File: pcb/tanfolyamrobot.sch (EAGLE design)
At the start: 80 parts, among them IC1 STM32F10XRXT6, IC2 7805, IC4 FT232RL, IC5 LD117AS33TR, M1 DRV8833, Q1 16MHz, Q2 BSS123, Q3 BSS123, Q4 BSS123, X2 PWR, X6 KUSBVX-BS1N

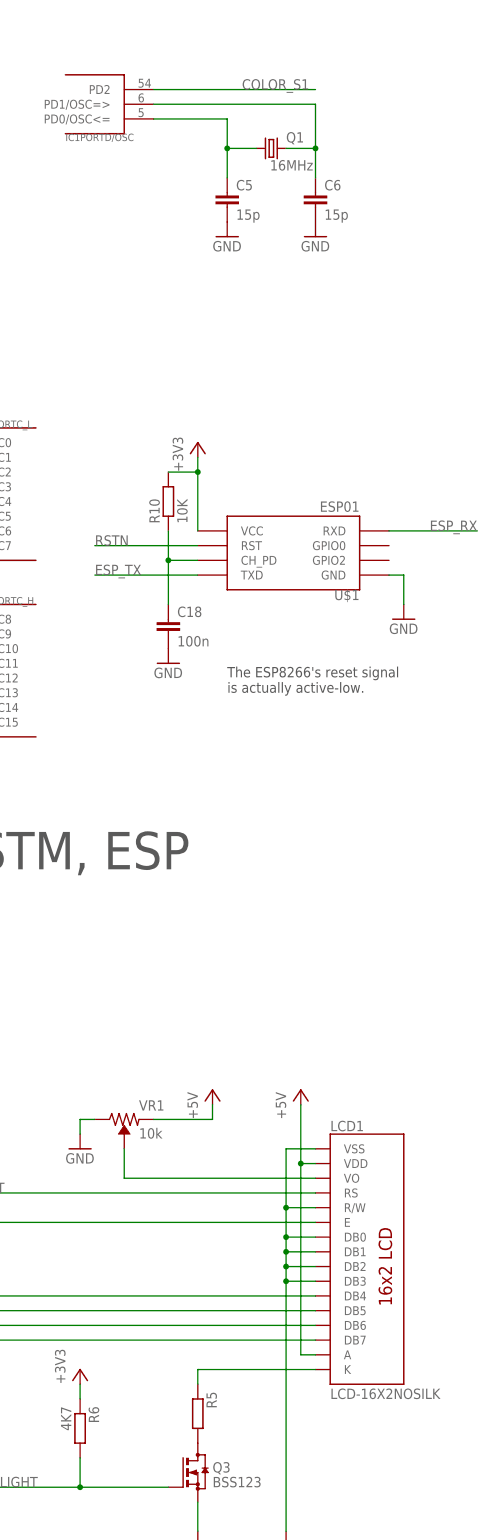
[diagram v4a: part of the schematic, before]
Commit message: changed xtal to smd resonator (#1)
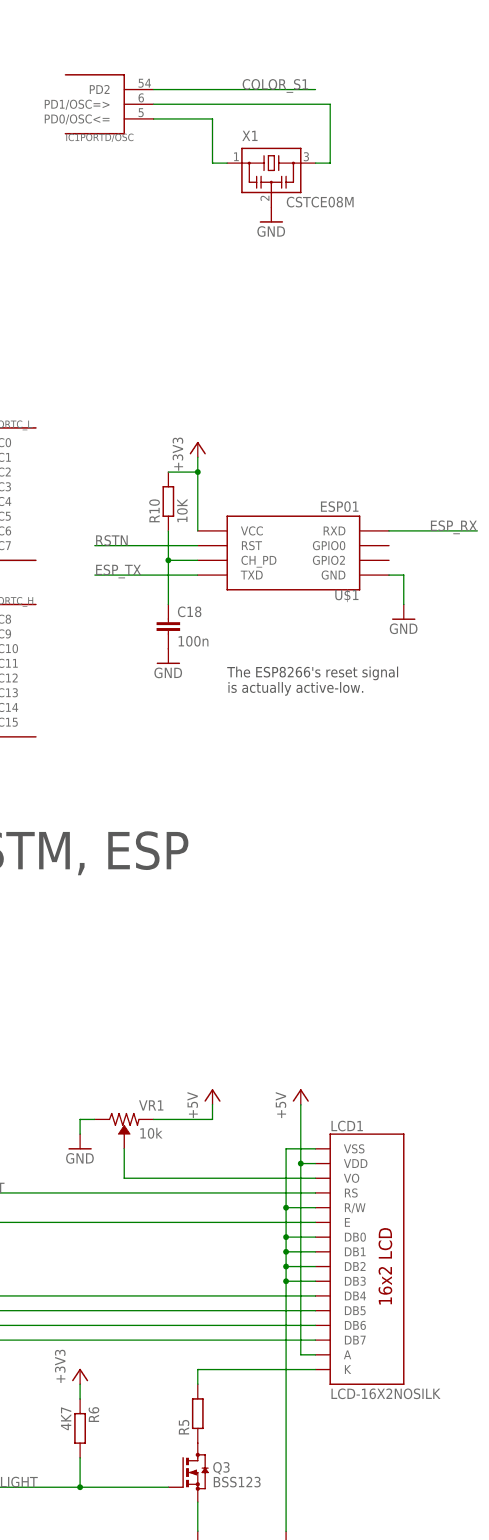
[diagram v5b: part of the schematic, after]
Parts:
- removed C5, C6: 15p, rcl:C-EUC0603
- removed Q1: 16MHz, crystal:CRYSTALHC49U-V
- added X1: CSTCE08M, resonator:MURATA_CSTCE
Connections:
- removed net LCD_K: LCD1.K, R5.1
- new net N$6: LCD1.K, R5.2
- net GND: now also X1.2; no longer C5.2, C6.2
- net N$1: now also R5.1; no longer R5.2
- net OSCIN: now also X1.1; no longer C5.1, Q1.1
- net OSCOUT: now also X1.3; no longer C6.1, Q1.2
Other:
- moved on the sheet: R5
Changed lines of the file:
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@@
 <part name="C3" library="rcl" library_urn="urn:adsk.eagle:library:334" deviceset="C-EU" device="C0603" package3d_urn="urn:adsk.eagle:package:23616/2" value="100n"/>
 <part name="C4" library="rcl" library_urn="urn:adsk.eagle:library:334" deviceset="C-EU" device="C0603" package3d_urn="urn:adsk.eagle:package:23616/2" value="100n"/>
-<part name="Q1" library="crystal" library_urn="urn:adsk.eagle:library:204" deviceset="CRYSTAL" device="HC49U-V" package3d_urn="urn:adsk.eagle:package:12075/1" value="16MHz"/>
-<part name="C5" library="rcl" library_urn="urn:adsk.eagle:library:334" deviceset="C-EU" device="C0603" package3d_urn="urn:adsk.eagle:package:23616/2" value="15p"/>
-<part name="C6" library="rcl" library_urn="urn:adsk.eagle:library:334" deviceset="C-EU" device="C0603" package3d_urn="urn:adsk.eagle:package:23616/2" value="15p"/>
-<part name="GND2" library="supply1" library_urn="urn:adsk.eagle:library:371" deviceset="GND" device=""/>
-<part name="GND3" library="supply1" library_urn="urn:adsk.eagle:library:371" deviceset="GND" device=""/>
 <part name="GND4" library="supply1" library_urn="urn:adsk.eagle:library:371" deviceset="GND" device=""/>
 <part name="+3V2" library="supply1" library_urn="urn:adsk.eagle:library:371" deviceset="+3V3" device=""/>
@@
 <part name="R27" library="rcl" library_urn="urn:adsk.eagle:library:334" deviceset="R-EU_" device="R0603" package3d_urn="urn:adsk.eagle:package:23555/3" value="0R"/>
 <part name="R28" library="rcl" library_urn="urn:adsk.eagle:library:334" deviceset="R-EU_" device="R0603" package3d_urn="urn:adsk.eagle:package:23555/3" value="0R"/>
+<part name="X1" library="resonator" deviceset="MURATA_CSTCE" device="" value="CSTCE08M"/>
+<part name="GND2" library="supply1" library_urn="urn:adsk.eagle:library:371" deviceset="GND" device=""/>
 </parts>
 <sheets>
@@
 <attribute name="VALUE" x="329.184" y="317.881" size="1.778" layer="96"/>
 </instance>
-<instance part="Q1" gate="G$1" x="487.68" y="322.58" smashed="yes">
-<attribute name="NAME" x="490.22" y="323.596" size="1.778" layer="95"/>
-<attribute name="VALUE" x="487.426" y="318.77" size="1.778" layer="96"/>
-</instance>
-<instance part="C5" gate="G$1" x="480.06" y="314.96" smashed="yes">
-<attribute name="NAME" x="481.584" y="315.341" size="1.778" layer="95"/>
-<attribute name="VALUE" x="481.584" y="310.261" size="1.778" layer="96"/>
-</instance>
-<instance part="C6" gate="G$1" x="495.3" y="314.96" smashed="yes">
-<attribute name="NAME" x="496.824" y="315.341" size="1.778" layer="95"/>
-<attribute name="VALUE" x="496.824" y="310.261" size="1.778" layer="96"/>
-</instance>
-<instance part="GND2" gate="1" x="480.06" y="307.34" smashed="yes">
-<attribute name="VALUE" x="477.52" y="304.8" size="1.778" layer="96"/>
-</instance>
-<instance part="GND3" gate="1" x="495.3" y="307.34" smashed="yes">
-<attribute name="VALUE" x="492.76" y="304.8" size="1.778" layer="96"/>
-</instance>
 <instance part="GND4" gate="1" x="391.16" y="309.88" smashed="yes">
 <attribute name="VALUE" x="388.62" y="307.34" size="1.778" layer="96"/>
@@
 <attribute name="VALUE" x="487.68" y="78.74" size="1.778" layer="96"/>
 </instance>
-<instance part="R5" gate="G$1" x="474.98" y="104.14" smashed="yes" rot="R270">
-<attribute name="NAME" x="476.4786" y="107.95" size="1.778" layer="95" rot="R270"/>
-<attribute name="VALUE" x="471.678" y="107.95" size="1.778" layer="96" rot="R270"/>
+<instance part="R5" gate="G$1" x="474.98" y="104.14" smashed="yes" rot="R90">
+<attribute name="NAME" x="473.4814" y="100.33" size="1.778" layer="95" rot="R90"/>
+<attribute name="VALUE" x="478.282" y="100.33" size="1.778" layer="96" rot="R90"/>
 </instance>
 <instance part="R6" gate="G$1" x="454.66" y="101.6" smashed="yes" rot="R270">
@@
 <attribute name="NAME" x="138.43" y="280.8986" size="1.778" layer="95"/>
 <attribute name="VALUE" x="144.526" y="280.924" size="1.778" layer="96"/>
+</instance>
+<instance part="X1" gate="G$1" x="487.68" y="320.04" smashed="yes">
+<attribute name="NAME" x="482.6" y="323.85" size="1.778" layer="95"/>
+<attribute name="VALUE" x="490.22" y="312.42" size="1.778" layer="96"/>
+</instance>
+<instance part="GND2" gate="1" x="487.68" y="309.88" smashed="yes">
+<attribute name="VALUE" x="485.14" y="307.34" size="1.778" layer="96"/>
 </instance>
 </instances>
@@
 </segment>
 <segment>
-<pinref part="C5" gate="G$1" pin="2"/>
-<pinref part="GND2" gate="1" pin="GND"/>
-</segment>
-<segment>
-<pinref part="C6" gate="G$1" pin="2"/>
-<pinref part="GND3" gate="1" pin="GND"/>
-</segment>
-<segment>
 <pinref part="C7" gate="G$1" pin="2"/>
 <wire x1="391.16" y1="314.96" x2="391.16" y2="317.5" width="0.1524" layer="91"/>
@@
 <pinref part="R9" gate="G$1" pin="2"/>
 <pinref part="GND35" gate="1" pin="GND"/>
+</segment>
+<segment>
+<pinref part="X1" gate="G$1" pin="2"/>
+<pinref part="GND2" gate="1" pin="GND"/>
 </segment>
 </net>
@@
 </segment>
 </net>
-<net name="OSCOUT" class="0">
-<segment>
-<wire x1="495.3" y1="330.2" x2="495.3" y2="322.58" width="0.1524" layer="91"/>
-<pinref part="Q1" gate="G$1" pin="2"/>
-<wire x1="490.22" y1="322.58" x2="495.3" y2="322.58" width="0.1524" layer="91"/>
-<wire x1="495.3" y1="322.58" x2="495.3" y2="317.5" width="0.1524" layer="91"/>
-<junction x="495.3" y="322.58"/>
-<pinref part="C6" gate="G$1" pin="1"/>
-<pinref part="IC1" gate="PORTD/OSC" pin="PD1/OSC=&gt;"/>
-<wire x1="467.36" y1="330.2" x2="495.3" y2="330.2" width="0.1524" layer="91"/>
-</segment>
-</net>
-<net name="OSCIN" class="0">
-<segment>
-<pinref part="Q1" gate="G$1" pin="1"/>
-<wire x1="485.14" y1="322.58" x2="480.06" y2="322.58" width="0.1524" layer="91"/>
-<wire x1="480.06" y1="322.58" x2="480.06" y2="317.5" width="0.1524" layer="91"/>
-<pinref part="C5" gate="G$1" pin="1"/>
-<wire x1="480.06" y1="327.66" x2="480.06" y2="322.58" width="0.1524" layer="91"/>
-<junction x="480.06" y="322.58"/>
-<pinref part="IC1" gate="PORTD/OSC" pin="PD0/OSC&lt;="/>
-<wire x1="467.36" y1="327.66" x2="480.06" y2="327.66" width="0.1524" layer="91"/>
-</segment>
-</net>
 <net name="SWD_SWO" class="0">
 <segment>
@@
 <wire x1="370.84" y1="238.76" x2="347.98" y2="238.76" width="0.1524" layer="91"/>
 <label x="347.98" y="238.76" size="1.778" layer="95"/>
-</segment>
-</net>
-<net name="LCD_K" class="0">
-<segment>
-<pinref part="R5" gate="G$1" pin="1"/>
-<wire x1="474.98" y1="109.22" x2="474.98" y2="111.76" width="0.1524" layer="91"/>
-<pinref part="LCD1" gate="G$1" pin="K"/>
-<wire x1="474.98" y1="111.76" x2="495.3" y2="111.76" width="0.1524" layer="91"/>
 </segment>
 </net>
@@
 </segment>
 </net>
-<net name="N$1" class="0">
-<segment>
-<pinref part="R5" gate="G$1" pin="2"/>
-<pinref part="Q3" gate="G$1" pin="D"/>
-</segment>
-</net>
 <net name="BOOT0" class="0">
 <segment>
@@
 </segment>
 </net>
+<net name="OSCIN" class="0">
+<segment>
+<pinref part="IC1" gate="PORTD/OSC" pin="PD0/OSC&lt;="/>
+<wire x1="467.36" y1="327.66" x2="477.52" y2="327.66" width="0.1524" layer="91"/>
+<wire x1="477.52" y1="327.66" x2="477.52" y2="320.04" width="0.1524" layer="91"/>
+<pinref part="X1" gate="G$1" pin="1"/>
+<wire x1="477.52" y1="320.04" x2="480.06" y2="320.04" width="0.1524" layer="91"/>
+</segment>
+</net>
+<net name="OSCOUT" class="0">
+<segment>
+<pinref part="IC1" gate="PORTD/OSC" pin="PD1/OSC=&gt;"/>
+<wire x1="467.36" y1="330.2" x2="497.84" y2="330.2" width="0.1524" layer="91"/>
+<wire x1="497.84" y1="330.2" x2="497.84" y2="320.04" width="0.1524" layer="91"/>
+<pinref part="X1" gate="G$1" pin="3"/>
+<wire x1="497.84" y1="320.04" x2="495.3" y2="320.04" width="0.1524" layer="91"/>
+</segment>
+</net>
+<net name="N$1" class="0">
+<segment>
+<pinref part="Q3" gate="G$1" pin="D"/>
+<pinref part="R5" gate="G$1" pin="1"/>
+</segment>
+</net>
+<net name="N$6" class="0">
+<segment>
+<pinref part="LCD1" gate="G$1" pin="K"/>
+<pinref part="R5" gate="G$1" pin="2"/>
+<wire x1="495.3" y1="111.76" x2="474.98" y2="111.76" width="0.1524" layer="91"/>
+<wire x1="474.98" y1="111.76" x2="474.98" y2="109.22" width="0.1524" layer="91"/>
+</segment>
+</net>

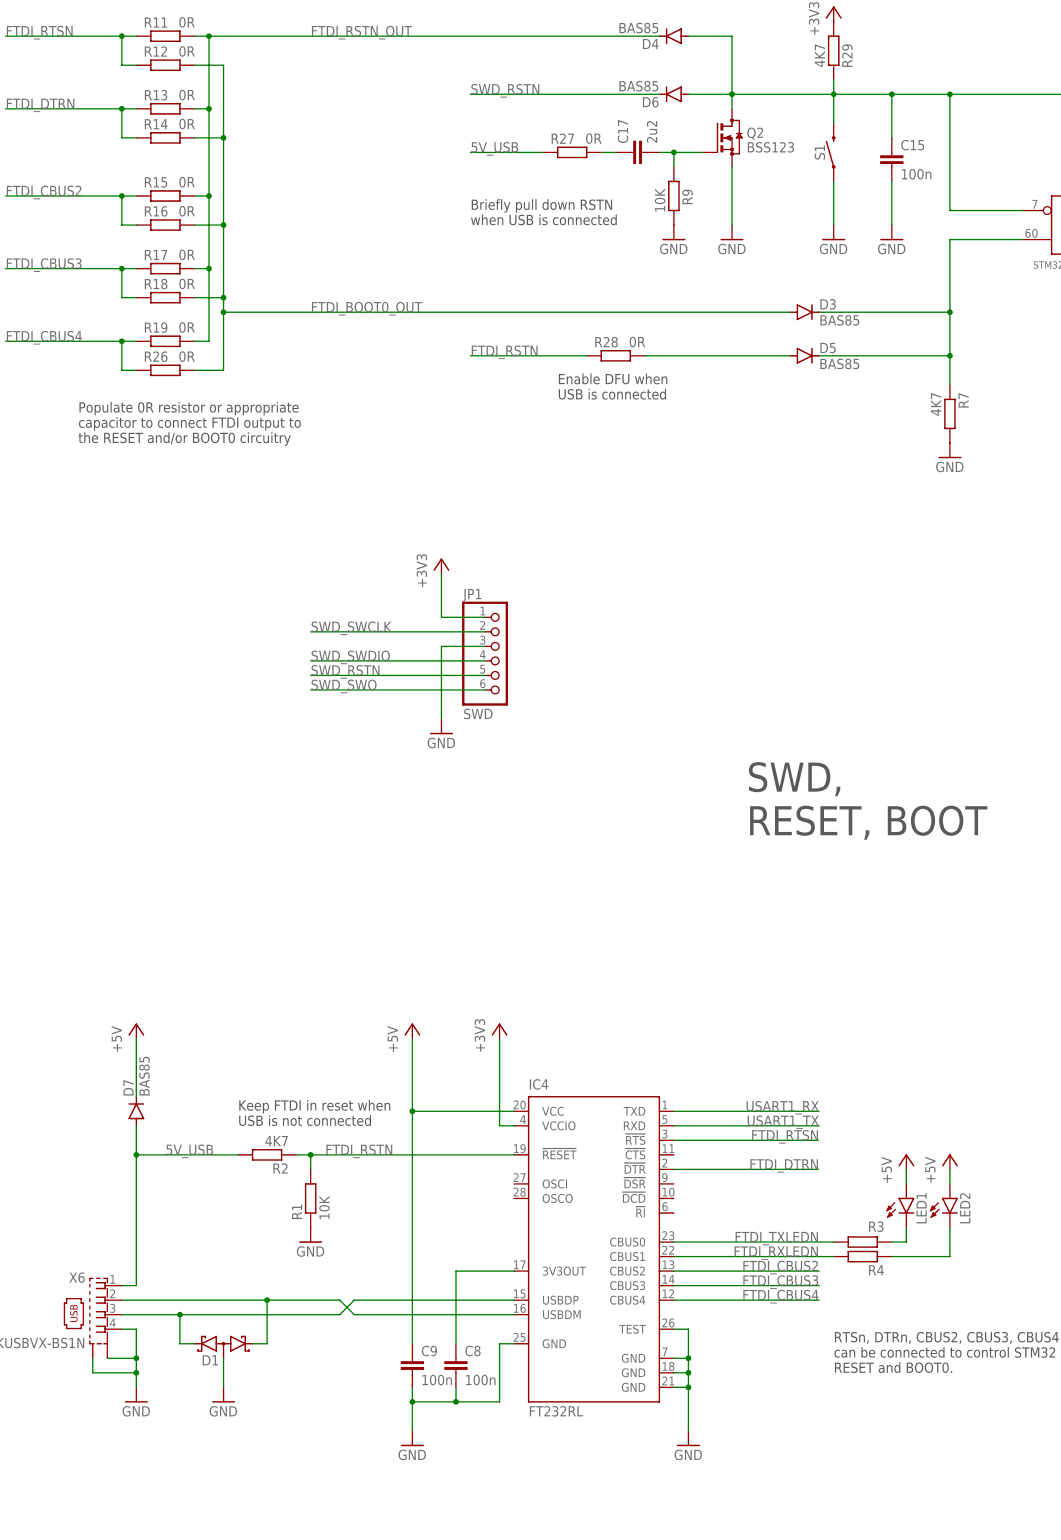
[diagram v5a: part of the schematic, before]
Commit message: changed USB transil diode packge (#1)
and also had to redesign a lot of stuff around the USB connector and FTDI chip
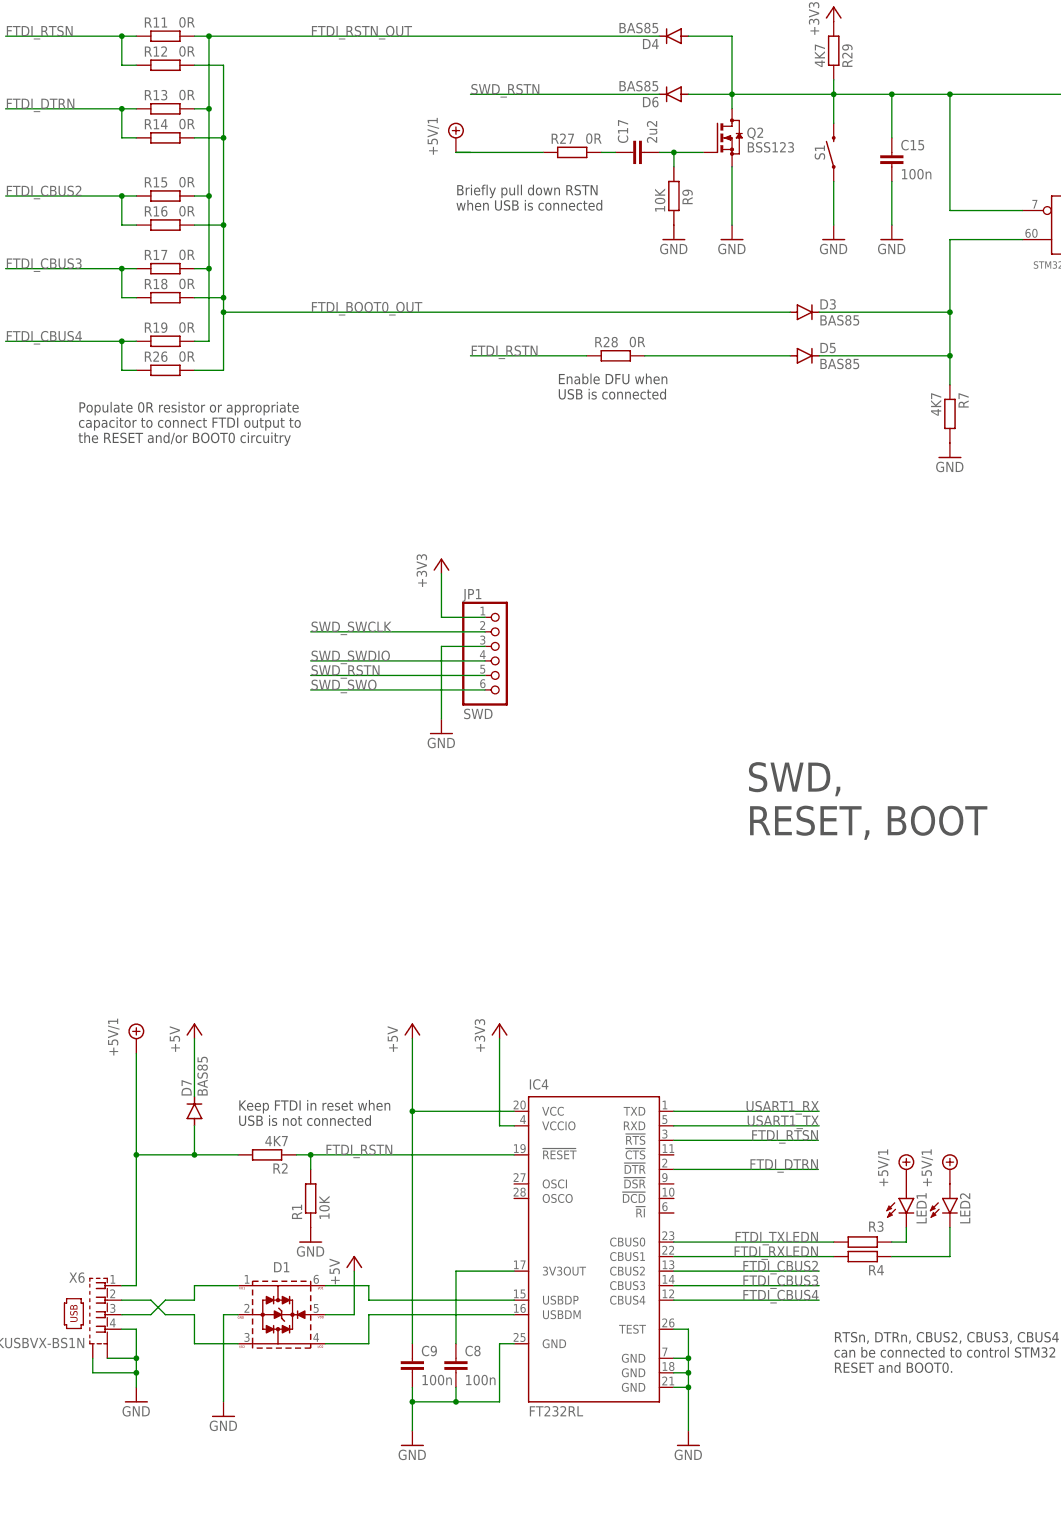
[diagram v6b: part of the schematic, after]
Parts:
- D1: value BAS40-06 -> 5Vdc; device diode:BAS40-06 -> Wurth_EMC Components_WE-TVS:WE-TVS-HS_SOT23-6L_82400102
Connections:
- net N$5 renamed FTDI_TXLEDN_R
- net N$7 renamed FTDI_RXLEDN_R
- removed net 5V_USB: D7.A, R2.2, R27.1, X6.1
- new net +5V/1: D7.A, LED1.A, LED2.A, R2.2, R27.1, X6.1
- new net USB_DM: D1.I/O2, X6.2
- new net USB_DP: D1.I/O1, X6.3
- net +5V: now also D1.VDD; no longer LED1.A, LED2.A
- net GND: now also D1.GND; no longer D1.AA
- net USB_DM_FTDI: now also D1.I/O4; no longer D1.K1, X6.2
- net USB_DP_FTDI: now also D1.I/O3; no longer D1.K2, X6.3
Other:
- moved on the sheet: D7

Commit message: cosmetic changes (#1)
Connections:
- net N$3 renamed ESP_CHPD
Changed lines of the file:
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@@
 </segment>
 </net>
-<net name="N$3" class="0">
+<net name="ESP_CHPD" class="0">
 <segment>
 <pinref part="U$1" gate="G$1" pin="CH_PD"/>
